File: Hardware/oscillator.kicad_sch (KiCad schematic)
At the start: 3 parts, among them Y1 ABM8G-48.000MHZ

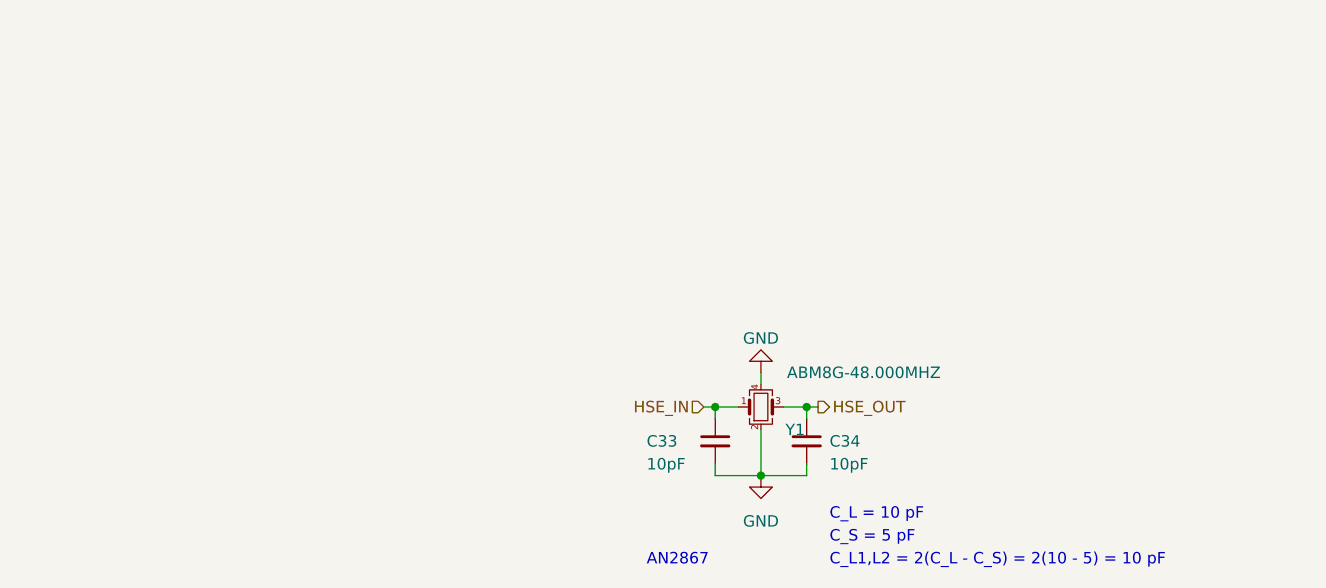
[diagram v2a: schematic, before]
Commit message: Created new hardware version 2.0
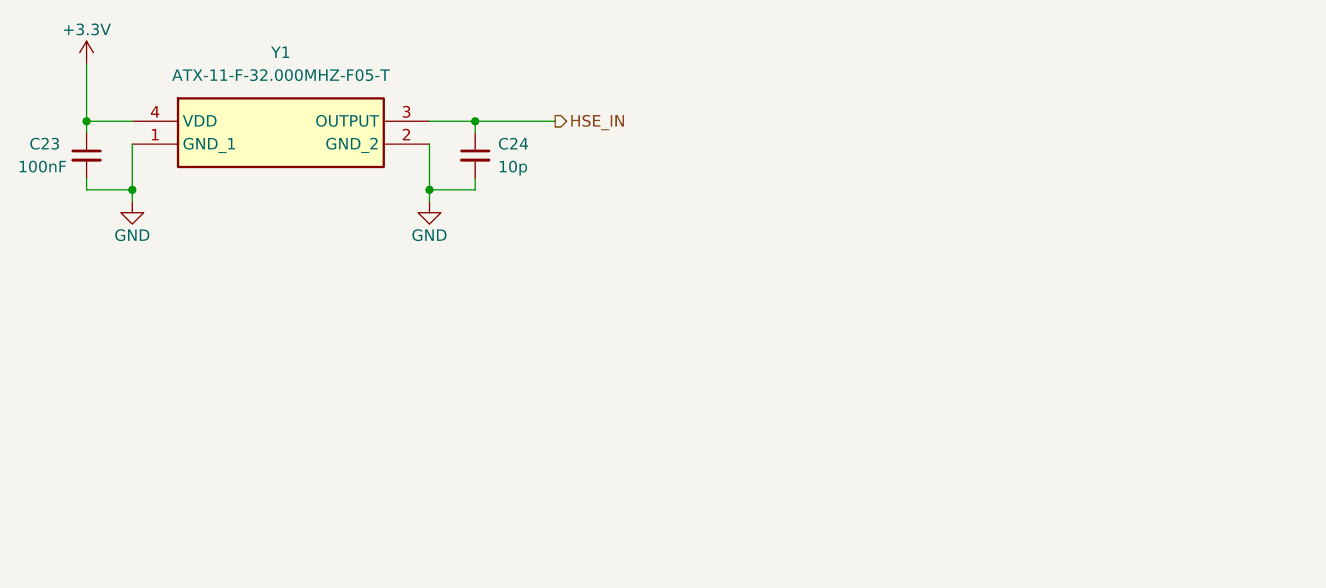
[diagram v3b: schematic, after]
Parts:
- removed C33, C34: 10pF, Capacitor_SMD:C_0402_1005Metric_Pad0.74x0.62mm_HandSolder, symbol Device:C_Small
- removed Y1: ABM8G-48.000MHZ, Crystal:Crystal_SMD_Abracon_ABM8G-4Pin_3.2x2.5mm, symbol Device:Crystal_GND24_Small
- added C23: 100nF, Capacitor_SMD:C_0603_1608Metric_Pad1.08x0.95mm_HandSolder, symbol Device:C_Small
- added C24: 10p, Capacitor_SMD:C_0603_1608Metric_Pad1.08x0.95mm_HandSolder, symbol Device:C_Small
- added Y1: ATX-11-F-32.000MHZ-F05-T, Samacsys:ATX11F32000MHZF05T, symbol Samacsys:ATX-11-F-32.000MHZ-F05-T
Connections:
- net GND: now also C23.2, C24.2, Y1.1 (GND_1), Y1.2 (GND_2)
- net HSE_IN: now also C24.1, Y1.3 (OUTPUT)
- new net +3.3V: C23.1, Y1.4 (VDD)
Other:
- note removed: "AN2867"
- note removed: "C_L = 10 pF"
- note removed: "C_L1,L2 = 2(C_L - C_S) = 2(10 - 5) = 10 pF"
- note removed: "C_S = 5 pF"
- company: Author: Szymon Kostrubiec -> (none)
- title: Oscillator -> (none)

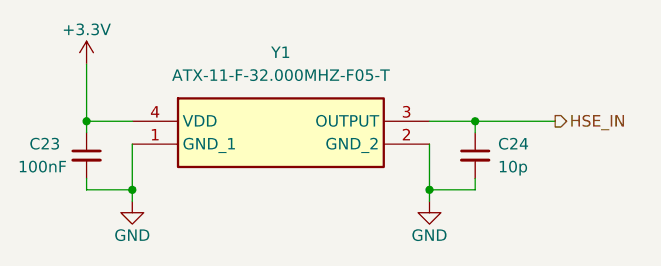
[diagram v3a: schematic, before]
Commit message: Changes in schematic, separated CAN buses, added XIAO Sense S3 DevBoard
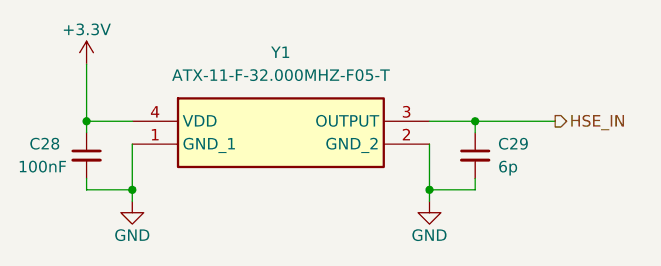
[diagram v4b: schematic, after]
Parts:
- C29: renamed from C24; value 10p -> 6p
- renumbered C23 to C28
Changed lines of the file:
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@@
 		(dnp no)
 		(fields_autoplaced yes)
-		(property "Reference" "C24"
+		(property "Reference" "C29"
 			(at 113.03 64.7762 0)
 			(effects
@@
 			)
 		)
-		(property "Value" "10p"
+		(property "Value" "6p"
 			(at 113.03 67.3162 0)
 			(effects
@@
 			(project ""
 				(path "/b652b05a-4e3d-4ad1-b032-18886abe7d45/55e35dc4-bd2c-4dc0-8f21-03116b82c791"
-					(reference "C24")
+					(reference "C29")
 					(unit 1)
 				)
@@
 		(on_board yes)
 		(dnp no)
-		(property "Reference" "C23"
+		(property "Reference" "C28"
 			(at 60.96 64.77 0)
 			(effects
@@
 			(project "PUTM_EV_Frontbox"
 				(path "/b652b05a-4e3d-4ad1-b032-18886abe7d45/55e35dc4-bd2c-4dc0-8f21-03116b82c791"
-					(reference "C23")
+					(reference "C28")
 					(unit 1)
 				)
@@
 		(on_board yes)
 		(dnp no)
-		(property "Reference" "#PWR061"
+		(property "Reference" "#PWR060"
 			(at 105.41 77.47 0)
 			(effects
@@
 			(project "PUTM_EV_Frontbox"
 				(path "/b652b05a-4e3d-4ad1-b032-18886abe7d45/55e35dc4-bd2c-4dc0-8f21-03116b82c791"
-					(reference "#PWR061")
+					(reference "#PWR060")
 					(unit 1)
 				)
@@
 		(dnp no)
 		(fields_autoplaced yes)
-		(property "Reference" "#PWR059"
+		(property "Reference" "#PWR058"
 			(at 67.31 59.69 0)
 			(effects
@@
 			(project "PUTM_EV_Frontbox"
 				(path "/b652b05a-4e3d-4ad1-b032-18886abe7d45/55e35dc4-bd2c-4dc0-8f21-03116b82c791"
-					(reference "#PWR059")
+					(reference "#PWR058")
 					(unit 1)
 				)
@@
 		(on_board yes)
 		(dnp no)
-		(property "Reference" "#PWR060"
+		(property "Reference" "#PWR059"
 			(at 72.39 77.47 0)
 			(effects
@@
 			(project "PUTM_EV_Frontbox"
 				(path "/b652b05a-4e3d-4ad1-b032-18886abe7d45/55e35dc4-bd2c-4dc0-8f21-03116b82c791"
-					(reference "#PWR060")
-					(unit 1)
-				)
+					(reference "#PWR059")
+					(unit 1)
+				)

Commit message: Changes in CAN section
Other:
- title: (none) -> FrontBox
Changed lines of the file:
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@@
 	(generator_version "9.0")
 	(paper "A4")
+	(title_block
+		(title "FrontBox")
+	)
 	(junction
 		(at 105.41 69.85)

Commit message: BOM update
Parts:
- C28, C29: Mouser Part Number (none) -> .
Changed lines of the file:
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@@
+			)
+		)
+		(property "Mouser Part Number" "."
+			(at 110.49 66.04 0)
+			(effects
+				(font
+					(size 1.27 1.27)
+				)
 			)
 		)
@@
 			)
 		)
+		(property "Mouser Part Number" "."
+			(at 67.31 66.04 0)
+			(effects
+				(font
+					(size 1.27 1.27)
+				)
+			)
+		)
